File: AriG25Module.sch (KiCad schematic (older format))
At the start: 12 parts

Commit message: Added MCP2200, serial to usb converter for debug.
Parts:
- added C?: 1uF, symbol C
- added C?: 100nF, symbol C
- added C? (x2): 6pF, symbol C
- added D? (x2): LED, symbol LED
- added P?: USB_OTG, symbol USB_OTG
- added R? (x2): R, symbol R
- added U?: MCP2200, symbol MCP2200
- added Y?: 12MHz, symbol Crystal_GND23
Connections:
- net +3V3: now also C?.1, C?.1, U?.1 (VDD)
- net GND: now also C?.1, C?.1, C?.2, C?.2, D?.1 (K), D?.1 (K), P?.5 (GND), P?.6 (shield), U?.20 (VSS), Y?.2, Y?.3
- net RX: now reaches U?.S13 (DTXD)
- net RX: now also U?.12 (RX)
- net TX: now reaches U?.S14 (DRXD)
- net TX: now also U?.10 (TX)
- new net: R?.1, U?.5 (GP7/TxLED)
- new net: R?.1, U?.6 (GP6/RxLED)
- new net: D?.2 (A), R?.2 (x2)
- new net D+: P?.3 (D+), U?.19 (D+)
- new net D-: P?.2 (D-), U?.18 (D-)
- new net OSC1: C?.2, U?.2 (OSC1), Y?.1
- new net OSC2: C?.2, U?.3 (OSC2), Y?.4
- new net VUSB: P?.1 (VBUS), U?.17 (VUSB)
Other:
- moved on the sheet: C?, U?

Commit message: I will merge and move the interfaces on a new sheet. Modified the schematic of a RJ45 Connector to be the same as the one used in Acme documentation.
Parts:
- added J?: RJ45-TRANSFO-NEW, symbol RJ45-TRANSFO-NEW
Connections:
- net labels added: ETH3V3, LINK, RX+, RX-, TRAFFIC, TX+, TX-
- wire segments 100 -> 118
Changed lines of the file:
@@
 LIBS:ic-cpu
 LIBS:MCP2200
+LIBS:w_connectors
 LIBS:E-GIF-M-Board-cache
 EELAYER 25 0
@@
 Wire Wire Line
 	8500 4700 8600 4700
+Text Label 5800 5250 0    50   ~ 0
+RX+
+Text Label 5800 5450 0    50   ~ 0
+RX-
+Text Label 5800 5750 0    50   ~ 0
+TX-
+Text Label 5800 5550 0    50   ~ 0
+TX+
+Text Label 5750 5950 0    50   ~ 0
+LINK
+Text Label 5750 6150 0    50   ~ 0
+TRAFFIC
+$Comp
+L GND #PWR?
+U 1 1 587EA960
+P 6100 6300
+F 0 "#PWR?" H 6100 6050 50  0001 C CNN
+F 1 "GND" H 6100 6150 50  0000 C CNN
+F 2 "" H 6100 6300 50  0000 C CNN
+F 3 "" H 6100 6300 50  0000 C CNN
+	1    6100 6300
+	1    0    0    -1
+$EndComp
+Text Label 4650 5900 0    50   ~ 0
+LINK
+Text Label 4650 5800 0    50   ~ 0
+TRAFFIC
+Wire Wire Line
+	4550 5800 4650 5800
+Wire Wire Line
+	4550 5900 4650 5900
+Text Label 4650 5600 0    50   ~ 0
+RX-
+Text Label 4650 5500 0    50   ~ 0
+RX+
+Text Label 4650 5300 0    50   ~ 0
+TX+
+Text Label 4650 5400 0    50   ~ 0
+TX-
+Wire Wire Line
+	4550 5300 4650 5300
+Wire Wire Line
+	4550 5400 4650 5400
+Wire Wire Line
+	4550 5500 4650 5500
+Wire Wire Line
+	4550 5600 4650 5600
+Text Label 4650 5700 0    50   ~ 0
+ETH3V3
+Text Label 5800 5350 0    50   ~ 0
+ETH3V3
+Text Label 5800 5650 0    50   ~ 0
+ETH3V3
+Wire Wire Line
+	4650 5700 4550 5700
+$Comp
+L RJ45-TRANSFO-NEW J?
+U 1 1 587FD01C
+P 7250 5750
+F 0 "J?" H 7350 6350 50  0000 L CNN
+F 1 "RJ45-TRANSFO-NEW" H 7200 6350 50  0000 R CNN
+F 2 "" H 7250 5750 50  0000 C CNN
+F 3 "" H 7250 5750 50  0000 C CNN
+	1    7250 5750
+	1    0    0    -1
+$EndComp
+Wire Wire Line
+	5800 5250 6150 5250
+Wire Wire Line
+	5800 5450 6150 5450
+Wire Wire Line
+	5800 5350 6150 5350
+Wire Wire Line
+	5800 5550 6150 5550
+Wire Wire Line
+	5800 5650 6150 5650
+Wire Wire Line
+	5800 5750 6150 5750
+Wire Wire Line
+	6150 5950 5750 5950
+Wire Wire Line
+	6150 6150 5750 6150
+Wire Wire Line
+	6150 6050 6100 6050
+Wire Wire Line
+	6100 6050 6100 6300
+Wire Wire Line
+	6100 6250 6150 6250
+Connection ~ 6100 6250
 $EndSCHEMATC

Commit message: Moved and connected the Debug, MicroSD and EthernetIN(EthIN) in the Interfaces schematic.
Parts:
- removed C? (x2): 1uF, symbol C
- removed C? (x2): 100nF, symbol C
- removed C? (x2): 6pF, symbol C
- removed CON?: Micro_SD_Card, symbol Micro_SD_Card
- removed D? (x2): LED, symbol LED
- removed J?: RJ45-TRANSFO-NEW, symbol RJ45-TRANSFO-NEW
- removed P?: USB_OTG, symbol USB_OTG
- removed R? (x2): R, symbol R
- removed U?: MCP2200, symbol MCP2200
- removed Y?: 12MHz, symbol Crystal_GND23
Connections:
- net labels added: CDA, CK, DA0, DA1, DA2, DA3, DRXD, DTXD, ETHLED1, ETHLED2, ETHRXN, ETHRXP, ETHTXN, ETHTXP
- net labels removed: CLK, CMD, D+, D-, DAT0, DAT1, DAT2, DAT3, LINK, OSC1, OSC2, RX, RX+, RX-, TRAFFIC, TX, TX+, TX-, VUSB
- wire segments 118 -> 50
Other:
- moved on the sheet: C?, U?

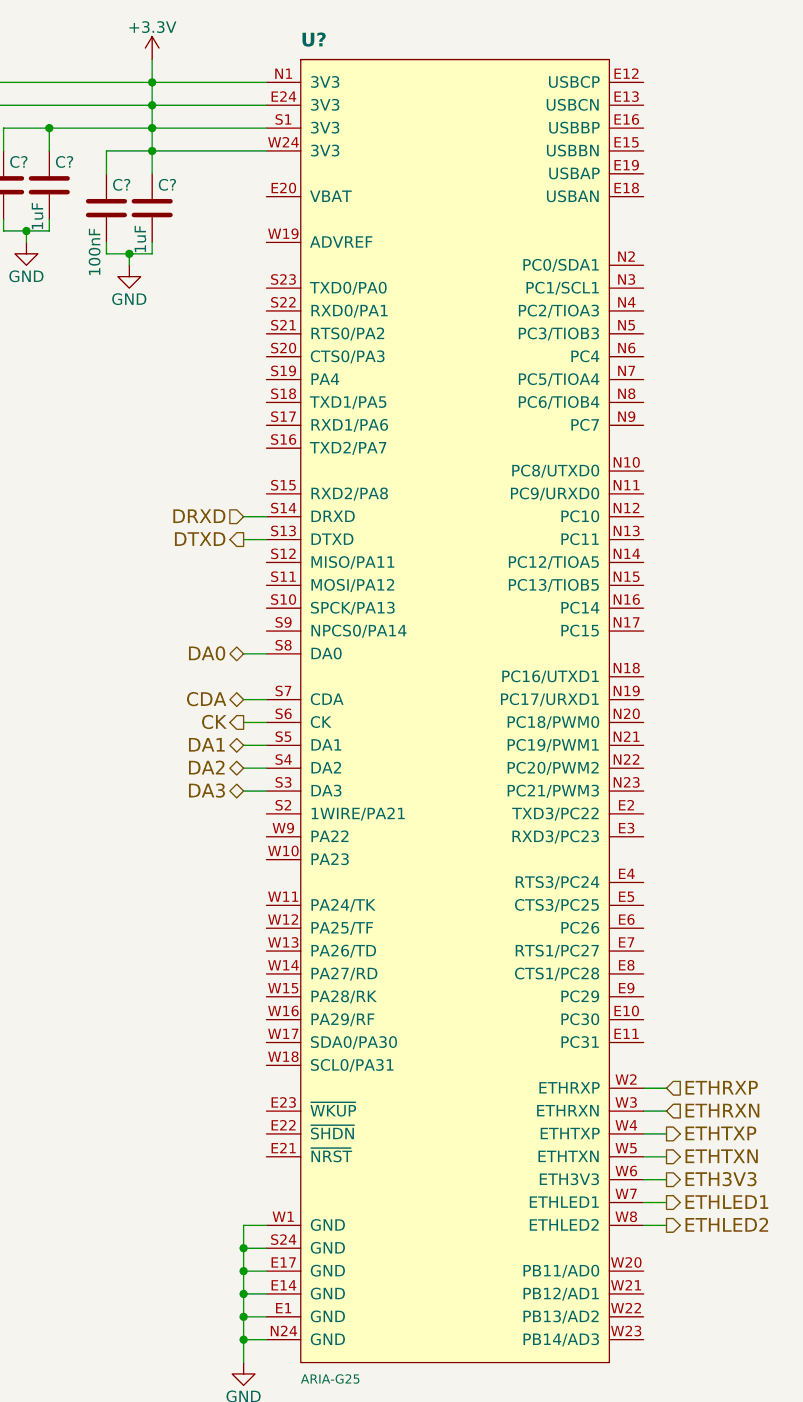
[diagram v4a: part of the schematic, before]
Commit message: Finished interfaces.
Finished MAX3232 serial to RS232 interface.
Finished ST3485 serial to RS485 interface.
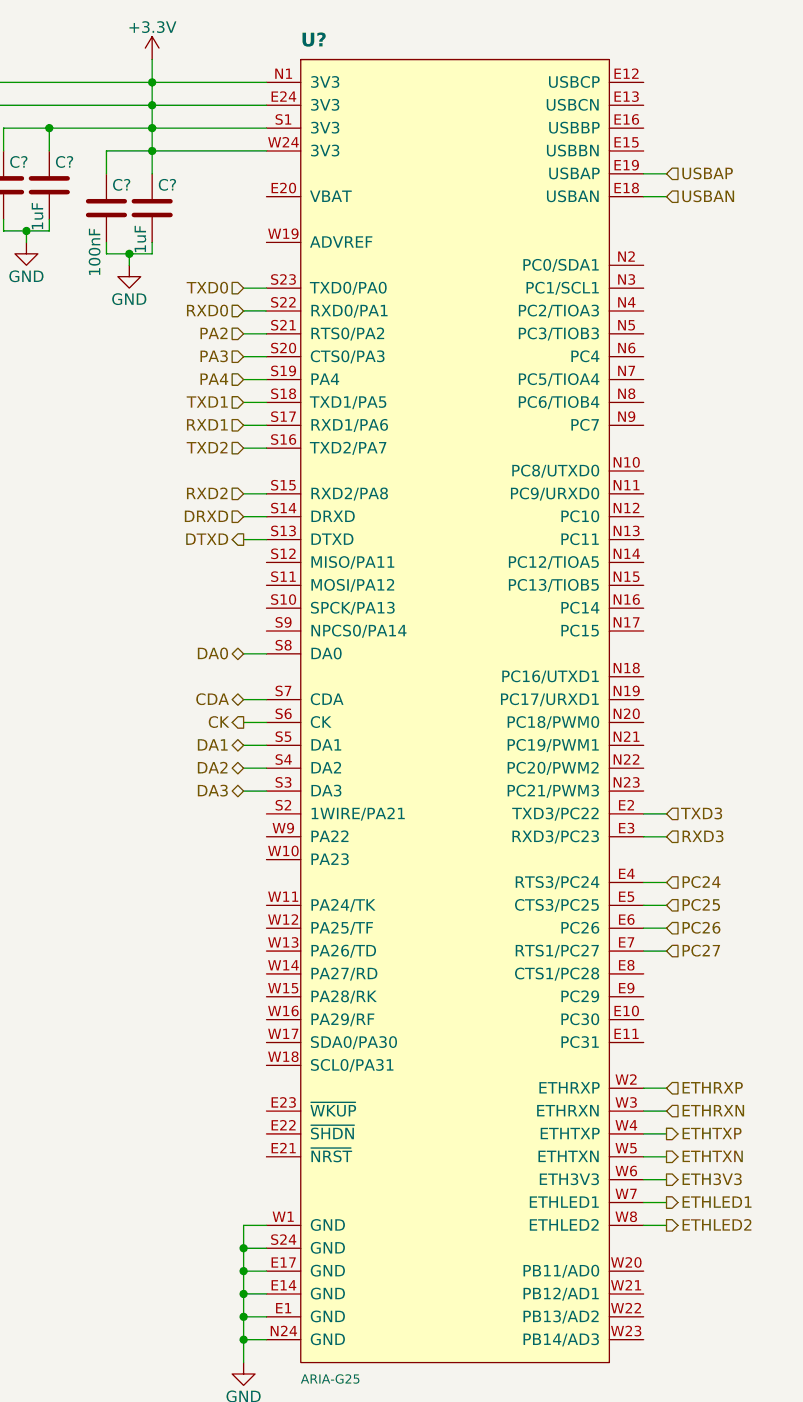
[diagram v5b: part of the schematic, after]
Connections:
- net USBAN: now reaches U?.E18 (USBAN)
- net USBAP: now reaches U?.E19 (USBAP)
- net TXD3: now reaches U?.E2 (TXD3/PC22)
- net RXD3: now reaches U?.E3 (RXD3/PC23)
- net PC24: now reaches U?.E4 (RTS3/PC24)
- net PC25: now reaches U?.E5 (CTS3/PC25)
- net PC26: now reaches U?.E6 (PC26)
- net PC27: now reaches U?.E7 (RTS1/PC27)
- net RXD2: now reaches U?.S15 (RXD2/PA8)
- net TXD2: now reaches U?.S16 (TXD2/PA7)
- net RXD1: now reaches U?.S17 (RXD1/PA6)
- net TXD1: now reaches U?.S18 (TXD1/PA5)
- net PA4: now reaches U?.S19 (PA4)
- net PA3: now reaches U?.S20 (CTS0/PA3)
- net PA2: now reaches U?.S21 (RTS0/PA2)
- net RXD0: now reaches U?.S22 (RXD0/PA1)
- net TXD0: now reaches U?.S23 (TXD0/PA0)
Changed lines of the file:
@@
 LIBS:MCP2200
 LIBS:w_connectors
+LIBS:max-lin
 LIBS:E-GIF-M-Board-cache
 EELAYER 25 0
@@
 $Descr A4 11693 8268
 encoding utf-8
-Sheet 3 5
+Sheet 3 7
 Title ""
 Date ""
@@
 $EndComp
 $Comp
-L GND #PWR?
+L GND #PWR014
 U 1 1 587D3F4F
 P 2050 1900
-F 0 "#PWR?" H 2050 1650 50  0001 C CNN
+F 0 "#PWR014" H 2050 1650 50  0001 C CNN
 F 1 "GND" H 2050 1750 50  0000 C CNN
 F 2 "" H 2050 1900 50  0000 C CNN
@@
 $EndComp
 $Comp
-L GND #PWR?
+L GND #PWR015
 U 1 1 587D3F7C
 P 2500 2000
-F 0 "#PWR?" H 2500 1750 50  0001 C CNN
+F 0 "#PWR015" H 2500 1750 50  0001 C CNN
 F 1 "GND" H 2500 1850 50  0000 C CNN
 F 2 "" H 2500 2000 50  0000 C CNN
@@
 $EndComp
 $Comp
-L GND #PWR?
+L GND #PWR016
 U 1 1 587D3FA2
 P 2950 2100
-F 0 "#PWR?" H 2950 1850 50  0001 C CNN
+F 0 "#PWR016" H 2950 1850 50  0001 C CNN
 F 1 "GND" H 2950 1950 50  0000 C CNN
 F 2 "" H 2950 2100 50  0000 C CNN
@@
 $EndComp
 $Comp
-L GND #PWR?
+L GND #PWR017
 U 1 1 587D3FC8
 P 3400 2200
-F 0 "#PWR?" H 3400 1950 50  0001 C CNN
+F 0 "#PWR017" H 3400 1950 50  0001 C CNN
 F 1 "GND" H 3400 2050 50  0000 C CNN
 F 2 "" H 3400 2200 50  0000 C CNN
@@
 $EndComp
 $Comp
-L +3.3V #PWR?
+L +3.3V #PWR018
 U 1 1 587D41CA
 P 3500 1300
-F 0 "#PWR?" H 3500 1150 50  0001 C CNN
+F 0 "#PWR018" H 3500 1150 50  0001 C CNN
 F 1 "+3.3V" H 3500 1440 50  0000 C CNN
 F 2 "" H 3500 1300 50  0000 C CNN
@@
 Connection ~ 3500 1600
 $Comp
-L GND #PWR?
+L GND #PWR019
 U 1 1 587D4706
 P 3900 7000
-F 0 "#PWR?" H 3900 6750 50  0001 C CNN
+F 0 "#PWR019" H 3900 6750 50  0001 C CNN
 F 1 "GND" H 3900 6850 50  0000 C CNN
 F 2 "" H 3900 7000 50  0000 C CNN
@@
 	4000 6900 3900 6900
 Connection ~ 3900 6900
-Text HLabel 3900 3900 0    60   BiDi ~ 0
+Text HLabel 3900 3900 0    50   BiDi ~ 0
 DA0
-Text HLabel 3900 4100 0    60   BiDi ~ 0
+Text HLabel 3900 4100 0    50   BiDi ~ 0
 CDA
-Text HLabel 3900 4200 0    60   Output ~ 0
+Text HLabel 3900 4200 0    50   Output ~ 0
 CK
-Text HLabel 3900 4300 0    60   BiDi ~ 0
+Text HLabel 3900 4300 0    50   BiDi ~ 0
 DA1
-Text HLabel 3900 4400 0    60   BiDi ~ 0
+Text HLabel 3900 4400 0    50   BiDi ~ 0
 DA2
-Text HLabel 3900 4500 0    60   BiDi ~ 0
+Text HLabel 3900 4500 0    50   BiDi ~ 0
 DA3
 Wire Wire Line
@@
 Wire Wire Line
 	3900 4500 4000 4500
-Text HLabel 3900 3300 0    60   Input ~ 0
+Text HLabel 3900 3300 0    50   Input ~ 0
 DRXD
-Text HLabel 3900 3400 0    60   Output ~ 0
+Text HLabel 3900 3400 0    50   Output ~ 0
 DTXD
 Wire Wire Line
@@
 Wire Wire Line
 	3900 3400 4000 3400
-Text HLabel 5750 5800 2    60   Input ~ 0
+Text HLabel 5750 5800 2    50   Input ~ 0
 ETHRXP
-Text HLabel 5750 5900 2    60   Input ~ 0
+Text HLabel 5750 5900 2    50   Input ~ 0
 ETHRXN
-Text HLabel 5750 6000 2    60   Output ~ 0
+Text HLabel 5750 6000 2    50   Output ~ 0
 ETHTXP
-Text HLabel 5750 6100 2    60   Output ~ 0
+Text HLabel 5750 6100 2    50   Output ~ 0
 ETHTXN
-Text HLabel 5750 6200 2    60   Output ~ 0
+Text HLabel 5750 6200 2    50   Output ~ 0
 ETH3V3
-Text HLabel 5750 6300 2    60   Output ~ 0
+Text HLabel 5750 6300 2    50   Output ~ 0
 ETHLED1
-Text HLabel 5750 6400 2    60   Output ~ 0
+Text HLabel 5750 6400 2    50   Output ~ 0
 ETHLED2
 Wire Wire Line
@@
 Wire Wire Line
 	5650 6400 5750 6400
+Text HLabel 3900 3200 0    50   Input ~ 0
+RXD2
+Text HLabel 3900 3000 0    50   Input ~ 0
+TXD2
+Text HLabel 3900 2900 0    50   Input ~ 0
+RXD1
+Text HLabel 3900 2800 0    50   Input ~ 0
+TXD1
+Text HLabel 3900 2400 0    50   Input ~ 0
+RXD0
+Text HLabel 3900 2300 0    50   Input ~ 0
+TXD0
+Text HLabel 5750 4600 2    50   Input ~ 0
+TXD3
+Text HLabel 5750 4700 2    50   Input ~ 0
+RXD3
+Wire Wire Line
+	5650 4600 5750 4600
+Wire Wire Line
+	5650 4700 5750 4700
+Wire Wire Line
+	3900 2300 4000 2300
+Wire Wire Line
+	3900 2400 4000 2400
+Wire Wire Line
+	3900 2800 4000 2800
+Wire Wire Line
+	3900 2900 4000 2900
+Wire Wire Line
+	3900 3000 4000 3000
+Wire Wire Line
+	3900 3200 4000 3200
+Text HLabel 5750 1800 2    50   Input ~ 0
+USBAP
+Text HLabel 5750 1900 2    50   Input ~ 0
+USBAN
+Wire Wire Line
+	5650 1900 5750 1900
+Wire Wire Line
+	5650 1800 5750 1800
+Text HLabel 5750 4900 2    50   Input ~ 0
+PC24
+Text HLabel 5750 5000 2    50   Input ~ 0
+PC25
+Text HLabel 5750 5100 2    50   Input ~ 0
+PC26
+Text HLabel 5750 5200 2    50   Input ~ 0
+PC27
+Wire Wire Line
+	5650 5200 5750 5200
+Wire Wire Line
+	5650 5100 5750 5100
+Wire Wire Line
+	5650 5000 5750 5000
+Wire Wire Line
+	5650 4900 5750 4900
+Text HLabel 3900 2500 0    50   Input ~ 0
+PA2
+Text HLabel 3900 2600 0    50   Input ~ 0
+PA3
+Text HLabel 3900 2700 0    50   Input ~ 0
+PA4
+Wire Wire Line
+	3900 2500 4000 2500
+Wire Wire Line
+	3900 2600 4000 2600
+Wire Wire Line
+	3900 2700 4000 2700
 $EndSCHEMATC
